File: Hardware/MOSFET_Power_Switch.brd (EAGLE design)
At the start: 35.6 x 34.3 mm, 56 parts, among them J3 5.5x2.1mm Barrel, Q1 600mA/40V, Q2 100A/100V/6.8mΩ, U1 LMR14203

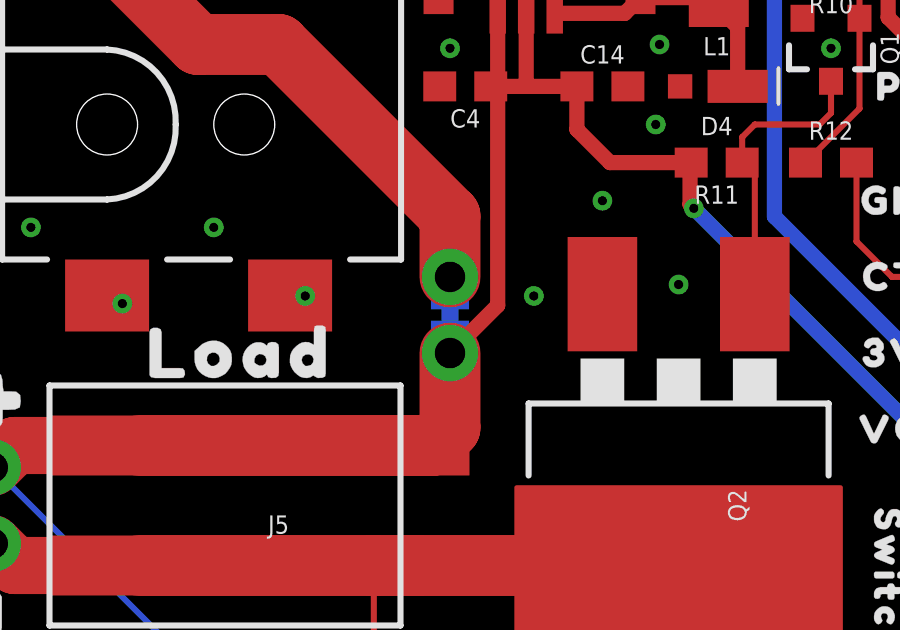
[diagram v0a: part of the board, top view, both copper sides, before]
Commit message: Update power jack
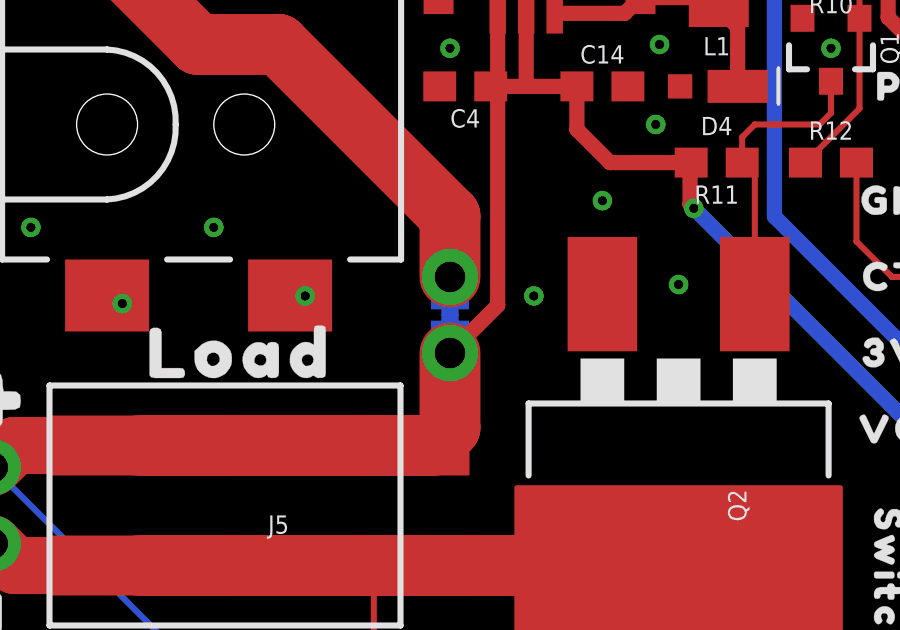
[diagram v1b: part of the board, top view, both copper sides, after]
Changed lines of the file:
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@@
 <layer number="154" name="FabDoc2" color="7" fill="1" visible="no" active="no"/>
 <layer number="155" name="FabDoc3" color="7" fill="1" visible="no" active="no"/>
+<layer number="156" name="gesam-Maß" color="7" fill="1" visible="no" active="no"/>
+<layer number="157" name="FaceMchng" color="7" fill="1" visible="no" active="no"/>
+<layer number="158" name="FaceMMeas" color="7" fill="1" visible="no" active="no"/>
+<layer number="159" name="Geh-Bear2" color="7" fill="1" visible="no" active="no"/>
+<layer number="160" name="Topologie" color="7" fill="1" visible="no" active="no"/>
+<layer number="161" name="tomplace2" color="7" fill="1" visible="no" active="no"/>
 <layer number="166" name="AntennaArea" color="7" fill="1" visible="no" active="no"/>
 <layer number="168" name="4mmHeightArea" color="7" fill="1" visible="no" active="no"/>
@@
 <layer number="250" name="Descript" color="3" fill="1" visible="no" active="no"/>
 <layer number="251" name="SMDround" color="12" fill="11" visible="no" active="no"/>
+<layer number="252" name="BR-BS" color="7" fill="1" visible="no" active="no"/>
 <layer number="253" name="Extra" color="7" fill="1" visible="no" active="no"/>
 <layer number="254" name="cooling" color="7" fill="1" visible="no" active="no"/>
@@
 <via x="8.636" y="19.431" extent="1-16" drill="0.3048"/>
 <contactref element="R1" pad="2"/>
+<wire x1="29.21" y1="25.4" x2="32.17" y2="27.94" width="0" layer="19" extent="1-1"/>
+<wire x1="28.26" y1="26.4" x2="29.21" y2="25.4" width="0" layer="19" extent="1-1"/>
+<wire x1="24.1808" y1="24.13" x2="28.26" y2="26.4" width="0" layer="19" extent="1-1"/>
+<wire x1="23.368" y1="22.86" x2="24.1808" y2="24.13" width="0" layer="19" extent="1-1"/>
+<wire x1="23.495" y1="25.527" x2="24.1808" y2="24.13" width="0" layer="19" extent="1-1"/>
+<wire x1="22.44" y1="24.13" x2="23.368" y2="22.86" width="0" layer="19" extent="1-1"/>
+<wire x1="21.59" y1="20.32" x2="23.368" y2="22.86" width="0" layer="19" extent="1-1"/>
+<wire x1="21.59" y1="17.205" x2="21.59" y2="20.32" width="0" layer="19" extent="1-1"/>
+<wire x1="19.304" y1="17.145" x2="21.59" y2="17.205" width="0" layer="19" extent="1-1"/>
+<wire x1="24.13" y1="17.526" x2="21.59" y2="17.205" width="0" layer="19" extent="1-1"/>
+<wire x1="21.336" y1="27.94" x2="23.495" y2="25.527" width="0" layer="19" extent="1-1"/>
+<wire x1="19.05" y1="29.3151" x2="21.336" y2="27.94" width="0" layer="19" extent="1-1"/>
+<wire x1="17.145" y1="27.94" x2="19.05" y2="29.3151" width="0" layer="19" extent="1-1"/>
+<wire x1="16.129" y1="27.09" x2="17.145" y2="27.94" width="0" layer="19" extent="1-1"/>
+<wire x1="16.51" y1="25.4" x2="16.129" y2="27.09" width="0" layer="19" extent="1-1"/>
+<wire x1="16.168" y1="24.13" x2="16.51" y2="25.4" width="0" layer="19" extent="1-1"/>
+<wire x1="23.495" y1="30.353" x2="21.336" y2="27.94" width="0" layer="19" extent="1-1"/>
+<wire x1="22.44" y1="31.75" x2="23.495" y2="30.353" width="0" layer="19" extent="1-1"/>
+<wire x1="26.3" y1="31.75" x2="23.495" y2="30.353" width="0" layer="19" extent="1-1"/>
+<wire x1="27.813" y1="31.75" x2="26.3" y2="31.75" width="0" layer="19" extent="1-1"/>
+<wire x1="21.59" y1="13.97" x2="21.59" y2="17.205" width="0" layer="19" extent="1-1"/>
+<wire x1="34.29" y1="20.32" x2="29.21" y2="25.4" width="0" layer="19" extent="1-1"/>
+<wire x1="11.684" y1="17.145" x2="19.304" y2="17.145" width="0" layer="19" extent="1-1"/>
+<wire x1="11.18" y1="17.16" x2="11.684" y2="17.145" width="0" layer="19" extent="1-1"/>
+<wire x1="8.636" y1="19.431" x2="11.18" y2="17.16" width="0" layer="19" extent="1-1"/>
+<wire x1="5.588" y1="16.891" x2="8.636" y2="19.431" width="0" layer="19" extent="1-1"/>
+<wire x1="5.08" y1="17.16" x2="5.588" y2="16.891" width="0" layer="19" extent="1-1"/>
+<wire x1="2.54" y1="19.431" x2="5.08" y2="17.16" width="0" layer="19" extent="1-1"/>
 </signal>
 <signal name="SDA1">
@@
 </board>
 </drawing>
+<compatibility>
+<note version="8.3" severity="warning">
+Since Version 8.3, EAGLE supports URNs for individual library
+assets (packages, symbols, and devices). The URNs of those assets
+will not be understood (or retained) with this version.
+</note>
+</compatibility>
 </eagle>
